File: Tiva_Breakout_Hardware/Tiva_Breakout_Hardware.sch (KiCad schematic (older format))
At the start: 10 parts, among them U1 TM4C129E_Launchpad

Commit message: Removed unnecessary connectors in schematic to reflect other boards
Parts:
- removed ConnA1, ConnA2: Molex_SL_09, MRDT_Connectors:MOLEX_SL_09_Horizontal, symbol MRDT_Connectors:Molex_SL_09
- removed ConnB1, ConnB2, ConnD1, ConnD2: Molex_SL_08, MRDT_Connectors:MOLEX_SL_08_Horizontal, symbol MRDT_Connectors:Molex_SL_08
- removed ConnC2: Molex_SL_10, MRDT_Connectors:MOLEX_SL_10_Horizontal, symbol MRDT_Connectors:Molex_SL_10
- added 12V_B2: Molex_SL_04, MRDT_Connectors:MOLEX_SL_04_Horizontal, symbol Tiva_Breakout_Hardware-rescue:Molex_SL_04-MRDT_Connectors
- added 30V_A1, 30V_B1: Molex_SL_07, MRDT_Connectors:MOLEX_SL_07_Horizontal, symbol Tiva_Breakout_Hardware-rescue:Molex_SL_07-MRDT_Connectors
- ConnC1: symbol MRDT_Connectors:Molex_SL_10 -> Tiva_Breakout_Hardware-rescue:Molex_SL_10-MRDT_Connectors
- ConnIN1: symbol MRDT_Connectors:Molex_SL_04 -> Tiva_Breakout_Hardware-rescue:Molex_SL_04-MRDT_Connectors
- U1: symbol MRDT_Shields:TM4C129E_Launchpad -> Tiva_Breakout_Hardware-rescue:TM4C129E_Launchpad-MRDT_Shields
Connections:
- wire segments 112 -> 50
- no-connect marks 2 -> 44

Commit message: rearranged pcb to account for physical layout
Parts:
- removed 30V_A1, 30V_B1: Molex_SL_07, MRDT_Connectors:MOLEX_SL_07_Horizontal, symbol Tiva_Breakout_Hardware-rescue:Molex_SL_07-MRDT_Connectors
- added Conn30V_L1, Conn30V_R1: Molex_SL_08, MRDT_Connectors:MOLEX_SL_08_Horizontal, symbol MRDT_Connectors:Molex_SL_08
- renumbered ConnC1 to ConnPCH_C2
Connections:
- no-connect marks 44 -> 46
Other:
- moved on the sheet: ConnPCH_C2, U1C
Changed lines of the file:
@@
 	3700 1950 4300 1950
 Wire Wire Line
-	3700 2050 4300 2050
-Wire Wire Line
-	5950 1350 6400 1350
-Wire Wire Line
-	5950 1450 6400 1450
-Wire Wire Line
-	5950 1550 6400 1550
-Wire Wire Line
-	5950 1650 6400 1650
-Wire Wire Line
-	5950 1750 6400 1750
-Wire Wire Line
-	5950 1850 6400 1850
-Wire Wire Line
-	5950 1950 6400 1950
-Wire Wire Line
-	5950 2050 6400 2050
-Wire Wire Line
-	5950 2150 6400 2150
-Wire Wire Line
-	5950 2250 6400 2250
+	6000 3000 6450 3000
+Wire Wire Line
+	6000 3100 6450 3100
+Wire Wire Line
+	6000 3200 6450 3200
+Wire Wire Line
+	6000 3300 6450 3300
+Wire Wire Line
+	6000 3400 6450 3400
+Wire Wire Line
+	6000 3500 6450 3500
+Wire Wire Line
+	6000 3600 6450 3600
+Wire Wire Line
+	6000 3700 6450 3700
+Wire Wire Line
+	6000 3800 6450 3800
+Wire Wire Line
+	6000 3900 6450 3900
 Wire Wire Line
 	4300 3200 3700 3200
@@
 L Tiva_Breakout_Hardware-rescue:TM4C129E_Launchpad-MRDT_Shields U1
 U 3 1 5D8F4A55
-P 6600 2300
-F 0 "U1" H 6650 3450 60  0000 L CNN
-F 1 "TM4C129E_Launchpad" V 6950 2350 60  0000 L CNN
-F 2 "MRDT_Shields:Tiva_Breakout" H 6600 2300 60  0001 C CNN
-F 3 "" H 6600 2300 60  0001 C CNN
-	3    6600 2300
+P 6650 2150
+F 0 "U1" H 6700 3300 60  0000 L CNN
+F 1 "TM4C129E_Launchpad" V 7000 2200 60  0000 L CNN
+F 2 "MRDT_Shields:Tiva_Breakout" H 6650 2150 60  0001 C CNN
+F 3 "" H 6650 2150 60  0001 C CNN
+	3    6650 2150
 	1    0    0    -1
 $EndComp
@@
 $EndComp
 $Comp
-L Tiva_Breakout_Hardware-rescue:Molex_SL_10-MRDT_Connectors ConnC1
+L Tiva_Breakout_Hardware-rescue:Molex_SL_10-MRDT_Connectors ConnPCH_C2
 U 1 1 5D908EEE
-P 5750 2300
-F 0 "ConnC1" H 5692 3497 60  0000 C CNN
-F 1 "Molex_SL_10" H 5692 3391 60  0000 C CNN
-F 2 "MRDT_Connectors:MOLEX_SL_10_Horizontal" H 5750 2800 60  0001 C CNN
-F 3 "" H 5750 2800 60  0001 C CNN
-	1    5750 2300
+P 5800 3950
+F 0 "ConnPCH_C2" H 5742 5147 60  0000 C CNN
+F 1 "Molex_SL_10" H 5742 5041 60  0000 C CNN
+F 2 "MRDT_Connectors:MOLEX_SL_10_Horizontal" H 5800 4450 60  0001 C CNN
+F 3 "" H 5800 4450 60  0001 C CNN
+	1    5800 3950
 	-1   0    0    -1
 $EndComp
@@
 NoConn ~ 8600 2150
 NoConn ~ 8600 2250
-NoConn ~ 6450 3000
-NoConn ~ 6450 3100
-NoConn ~ 6450 3200
-NoConn ~ 6450 3300
-NoConn ~ 6450 3400
-NoConn ~ 6450 3500
-NoConn ~ 6450 3600
-NoConn ~ 6450 3700
-NoConn ~ 6450 3800
-NoConn ~ 6450 3900
 NoConn ~ 8650 3900
 NoConn ~ 8650 3800
@@
 Text Notes 7800 850  0    197  ~ 39
 Unassigned
-$Comp
-L Tiva_Breakout_Hardware-rescue:Molex_SL_07-MRDT_Connectors 30V_A1
-U 1 1 5DBFC3B6
-P 950 2000
-F 0 "30V_A1" H 892 2897 60  0000 C CNN
-F 1 "Molex_SL_07" H 892 2791 60  0000 C CNN
-F 2 "MRDT_Connectors:MOLEX_SL_07_Horizontal" H 950 2200 60  0001 C CNN
-F 3 "" H 950 2200 60  0001 C CNN
-	1    950  2000
-	-1   0    0    -1
-$EndComp
-NoConn ~ 3700 2150
 NoConn ~ 1500 2150
+Wire Wire Line
+	1150 1350 1500 1350
+Wire Wire Line
+	1500 1450 1150 1450
+Wire Wire Line
+	1150 1550 1500 1550
+Wire Wire Line
+	1500 1650 1150 1650
+Wire Wire Line
+	1150 1750 1500 1750
+Wire Wire Line
+	1500 1850 1150 1850
+$Comp
+L MRDT_Connectors:Molex_SL_08 Conn30V_L1
+U 1 1 5DCE1DDF
+P 950 2100
+F 0 "Conn30V_L1" H 892 3097 60  0000 C CNN
+F 1 "Molex_SL_08" H 892 2991 60  0000 C CNN
+F 2 "MRDT_Connectors:MOLEX_SL_08_Horizontal" H 950 2400 60  0001 C CNN
+F 3 "" H 950 2400 60  0001 C CNN
+	1    950  2100
+	-1   0    0    -1
+$EndComp
+$Comp
+L MRDT_Connectors:Molex_SL_08 Conn30V_R1
+U 1 1 5DCE5C02
+P 4500 2200
+F 0 "Conn30V_R1" H 4628 2658 60  0000 L CNN
+F 1 "Molex_SL_08" H 4628 2552 60  0000 L CNN
+F 2 "MRDT_Connectors:MOLEX_SL_08_Horizontal" H 4500 2500 60  0001 C CNN
+F 3 "" H 4500 2500 60  0001 C CNN
+	1    4500 2200
+	1    0    0    -1
+$EndComp
+Wire Wire Line
+	3700 2050 4300 2050
+Wire Wire Line
+	3700 2150 4300 2150
+NoConn ~ 1500 1950
 NoConn ~ 1500 2050
-Wire Wire Line
-	1150 1350 1500 1350
-Wire Wire Line
-	1500 1450 1150 1450
-Wire Wire Line
-	1150 1550 1500 1550
-Wire Wire Line
-	1500 1650 1150 1650
-Wire Wire Line
-	1150 1750 1500 1750
-Wire Wire Line
-	1500 1850 1150 1850
-Wire Wire Line
-	1150 1950 1500 1950
-$Comp
-L Tiva_Breakout_Hardware-rescue:Molex_SL_07-MRDT_Connectors 30V_B1
-U 1 1 5DC09C1D
-P 4500 2100
-F 0 "30V_B1" H 4450 3000 60  0000 L CNN
-F 1 "Molex_SL_07" H 4300 2900 60  0000 L CNN
-F 2 "MRDT_Connectors:MOLEX_SL_07_Horizontal" H 4500 2300 60  0001 C CNN
-F 3 "" H 4500 2300 60  0001 C CNN
-	1    4500 2100
-	1    0    0    -1
-$EndComp
+NoConn ~ 1150 2050
+NoConn ~ 1150 1950
+NoConn ~ 6450 1200
+NoConn ~ 6450 1300
+NoConn ~ 6450 1400
+NoConn ~ 6450 1500
+NoConn ~ 6450 1600
+NoConn ~ 6450 1700
+NoConn ~ 6450 1800
+NoConn ~ 6450 1900
+NoConn ~ 6450 2000
+NoConn ~ 6450 2100
 $EndSCHEMATC

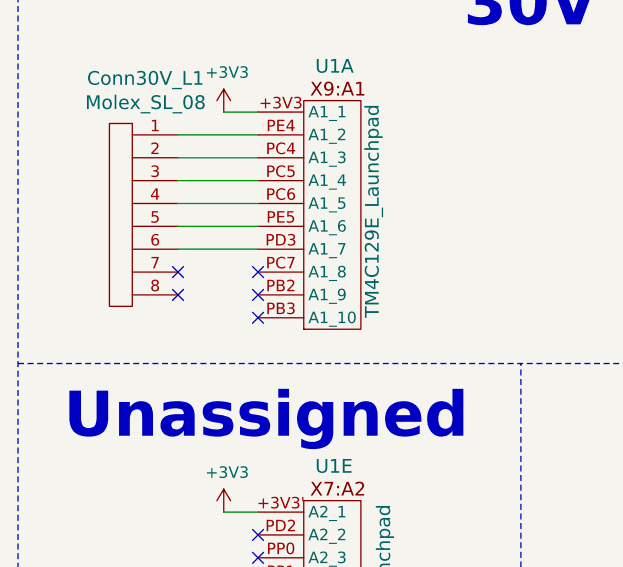
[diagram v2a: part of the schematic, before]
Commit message: In process of changing layout for smaller board
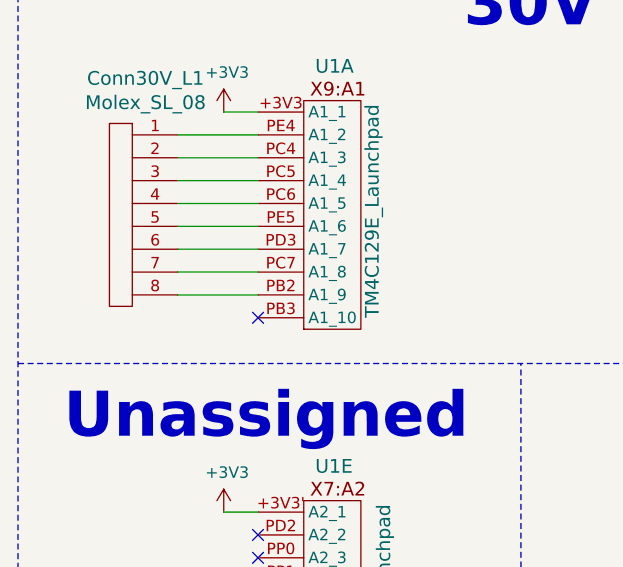
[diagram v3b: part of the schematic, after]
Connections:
- net at U1.PB2 (A1_9): now also Conn30V_L1.8
- net at U1.PC7 (A1_8): now also Conn30V_L1.7
- no-connect marks 46 -> 42
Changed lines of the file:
@@
 	1    0    0    -1
 $EndComp
-Wire Wire Line
-	3700 2050 4300 2050
-Wire Wire Line
-	3700 2150 4300 2150
-NoConn ~ 1500 1950
-NoConn ~ 1500 2050
-NoConn ~ 1150 2050
-NoConn ~ 1150 1950
 NoConn ~ 6450 1200
 NoConn ~ 6450 1300
@@
 NoConn ~ 6450 2000
 NoConn ~ 6450 2100
+Wire Wire Line
+	3700 2050 4300 2050
+Wire Wire Line
+	3700 2150 4300 2150
+Wire Wire Line
+	1150 1950 1500 1950
+Wire Wire Line
+	1150 2050 1500 2050
 $EndSCHEMATC

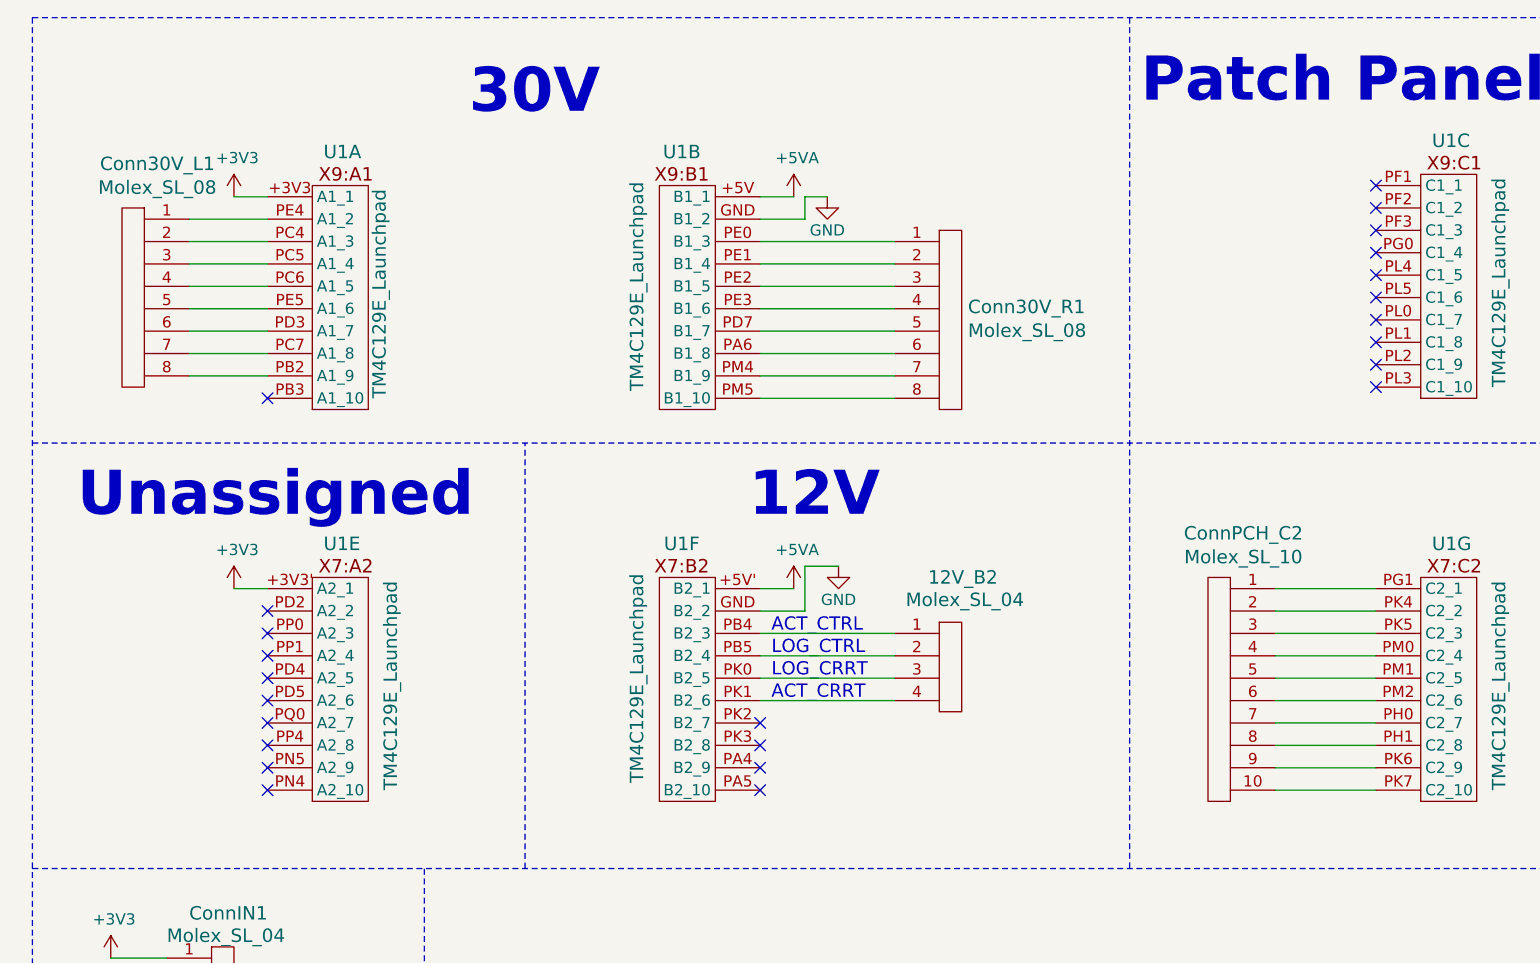
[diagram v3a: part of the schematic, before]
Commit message: New layout, as board is on left of others now. Changed pin assignments.
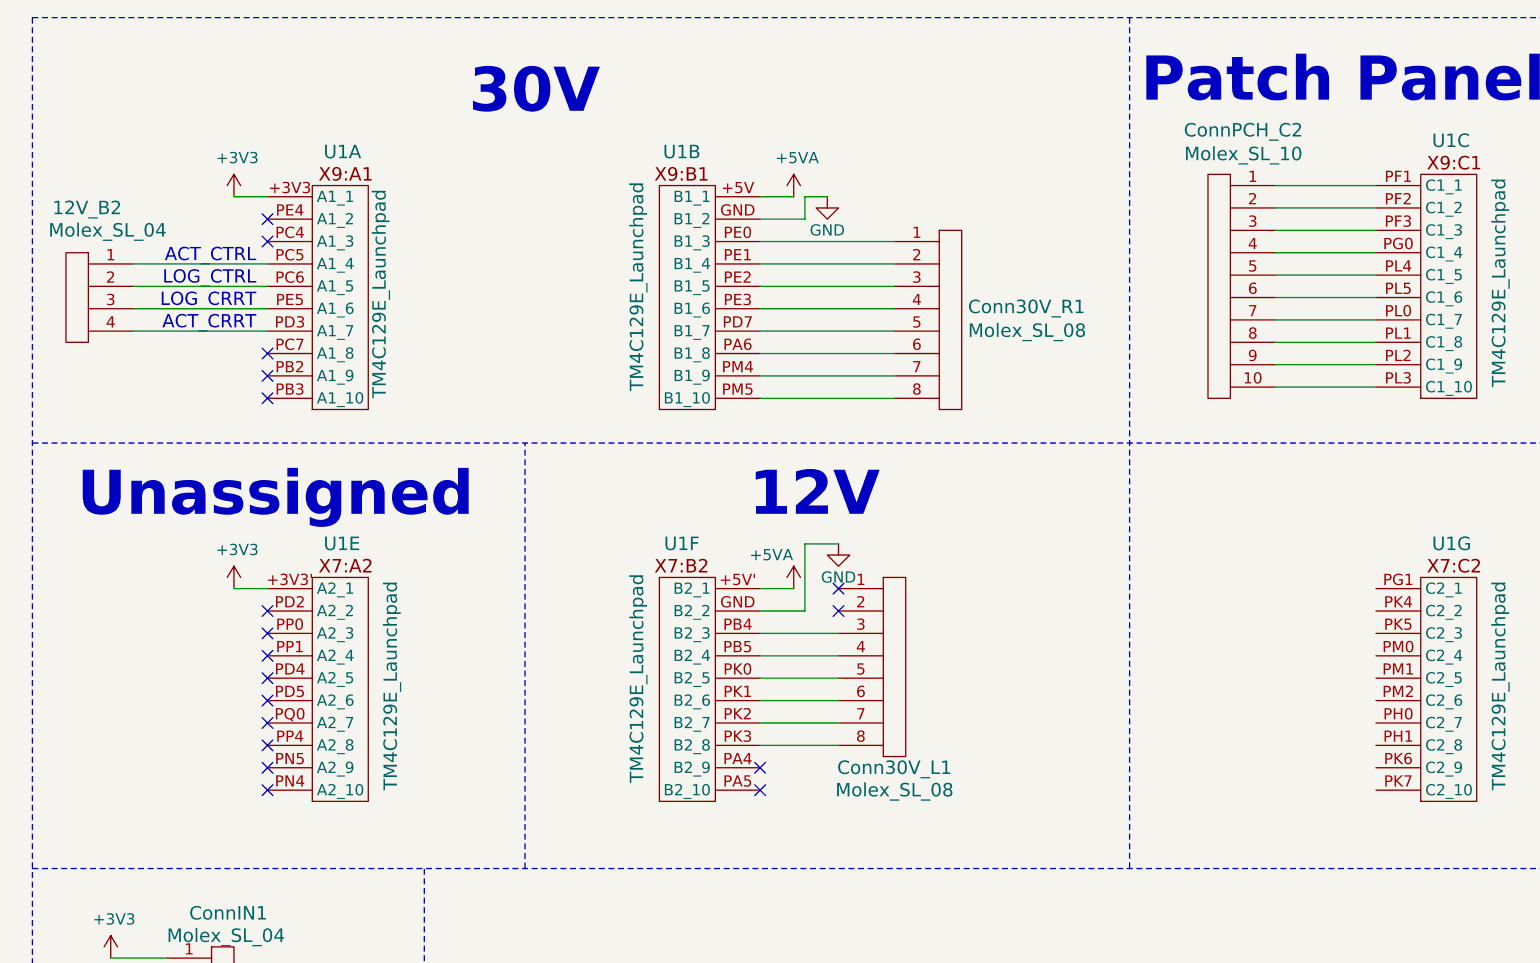
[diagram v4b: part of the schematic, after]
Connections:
- net at U1.PB2 (A1_9): no longer Conn30V_L1.8
- net at U1.PC4 (A1_3): no longer Conn30V_L1.2
- net at U1.PC5 (A1_4): now also 12V_B2.1; no longer Conn30V_L1.3
- net at U1.PC6 (A1_5): now also 12V_B2.2; no longer Conn30V_L1.4
- net at U1.PC7 (A1_8): no longer Conn30V_L1.7
- net at U1.PD3 (A1_7): now also 12V_B2.4; no longer Conn30V_L1.6
- net at U1.PE4 (A1_2): no longer Conn30V_L1.1
- net at U1.PE5 (A1_6): now also 12V_B2.3; no longer Conn30V_L1.5
- net at U1.PF1 (C1_1): now also ConnPCH_C2.1
- net at U1.PF2 (C1_2): now also ConnPCH_C2.2
- net at U1.PF3 (C1_3): now also ConnPCH_C2.3
- net at U1.PG0 (C1_4): now also ConnPCH_C2.4
- net at U1.PL0 (C1_7): now also ConnPCH_C2.7
- net at U1.PL1 (C1_8): now also ConnPCH_C2.8
- net at U1.PL2 (C1_9): now also ConnPCH_C2.9
- net at U1.PL3 (C1_10): now also ConnPCH_C2.10
- net at U1.PL4 (C1_5): now also ConnPCH_C2.5
- net at U1.PL5 (C1_6): now also ConnPCH_C2.6
- net at U1.PB4 (B2_3): now also Conn30V_L1.3; no longer 12V_B2.1
- net at U1.PB5 (B2_4): now also Conn30V_L1.4; no longer 12V_B2.2
- net at U1.PK0 (B2_5): now also Conn30V_L1.5; no longer 12V_B2.3
- net at U1.PK1 (B2_6): now also Conn30V_L1.6; no longer 12V_B2.4
- net at U1.PK2 (B2_7): now also Conn30V_L1.7
- net at U1.PK3 (B2_8): now also Conn30V_L1.8
- net at U1.PG1 (C2_1): no longer ConnPCH_C2.1
- net at U1.PH0 (C2_7): no longer ConnPCH_C2.7
- net at U1.PH1 (C2_8): no longer ConnPCH_C2.8
- net at U1.PK4 (C2_2): no longer ConnPCH_C2.2
- net at U1.PK5 (C2_3): no longer ConnPCH_C2.3
- net at U1.PK6 (C2_9): no longer ConnPCH_C2.9
- net at U1.PK7 (C2_10): no longer ConnPCH_C2.10
- net at U1.PM0 (C2_4): no longer ConnPCH_C2.4
- net at U1.PM1 (C2_5): no longer ConnPCH_C2.5
- net at U1.PM2 (C2_6): no longer ConnPCH_C2.6
- no-connect marks 42 -> 36
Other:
- moved on the sheet: 12V_B2, Conn30V_L1, ConnPCH_C2
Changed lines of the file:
@@
 Text Notes 800  5750 0    118  ~ 24
 Power Input
-NoConn ~ 8600 1750
 NoConn ~ 8650 3400
 $Comp
@@
 P 3850 3000
 F 0 "#PWR0104" H 3850 2850 50  0001 C CNN
-F 1 "+5VA" H 3865 3173 50  0000 C CNN
+F 1 "+5VA" H 3750 3150 50  0000 C CNN
 F 2 "" H 3850 3000 50  0001 C CNN
 F 3 "" H 3850 3000 50  0001 C CNN
@@
 L power:GND #PWR0110
 U 1 1 5D93847D
-P 4050 2900
-F 0 "#PWR0110" H 4050 2650 50  0001 C CNN
-F 1 "GND" H 4050 2750 50  0000 C CNN
-F 2 "" H 4050 2900 50  0001 C CNN
-F 3 "" H 4050 2900 50  0001 C CNN
-	1    4050 2900
+P 4050 2800
+F 0 "#PWR0110" H 4050 2550 50  0001 C CNN
+F 1 "GND" H 4050 2650 50  0000 C CNN
+F 2 "" H 4050 2800 50  0001 C CNN
+F 3 "" H 4050 2800 50  0001 C CNN
+	1    4050 2800
 	1    0    0    -1
 $EndComp
@@
 	3700 1950 4300 1950
 Wire Wire Line
-	6000 3000 6450 3000
-Wire Wire Line
-	6000 3100 6450 3100
-Wire Wire Line
-	6000 3200 6450 3200
-Wire Wire Line
-	6000 3300 6450 3300
-Wire Wire Line
-	6000 3400 6450 3400
-Wire Wire Line
-	6000 3500 6450 3500
-Wire Wire Line
-	6000 3600 6450 3600
-Wire Wire Line
-	6000 3700 6450 3700
-Wire Wire Line
-	6000 3800 6450 3800
-Wire Wire Line
-	6000 3900 6450 3900
-Wire Wire Line
-	4300 3200 3700 3200
-Wire Wire Line
-	3700 3300 4300 3300
-Wire Wire Line
-	3700 3400 4300 3400
-Wire Wire Line
-	3700 3500 4300 3500
+	6000 1200 6450 1200
+Wire Wire Line
+	6000 1300 6450 1300
+Wire Wire Line
+	6000 1400 6450 1400
+Wire Wire Line
+	6000 1500 6450 1500
+Wire Wire Line
+	6000 1600 6450 1600
+Wire Wire Line
+	6000 1700 6450 1700
+Wire Wire Line
+	6000 1800 6450 1800
+Wire Wire Line
+	6000 1900 6450 1900
+Wire Wire Line
+	6000 2000 6450 2000
+Wire Wire Line
+	6000 2100 6450 2100
 $Comp
 L Tiva_Breakout_Hardware-rescue:TM4C129E_Launchpad-MRDT_Shields U1
@@
 	3    6650 2150
 	1    0    0    -1
-$EndComp
-$Comp
-L Tiva_Breakout_Hardware-rescue:TM4C129E_Launchpad-MRDT_Shields U1
-U 4 1 5D8F6A14
-P 8400 2300
-F 0 "U1" H 8550 3450 60  0000 C CNN
-F 1 "TM4C129E_Launchpad" V 8750 2850 60  0000 C CNN
-F 2 "MRDT_Shields:Tiva_Breakout" H 8400 2300 60  0001 C CNN
-F 3 "" H 8400 2300 60  0001 C CNN
-	4    8400 2300
-	-1   0    0    -1
 $EndComp
 $Comp
@@
 L Tiva_Breakout_Hardware-rescue:Molex_SL_10-MRDT_Connectors ConnPCH_C2
 U 1 1 5D908EEE
-P 5800 3950
-F 0 "ConnPCH_C2" H 5742 5147 60  0000 C CNN
-F 1 "Molex_SL_10" H 5742 5041 60  0000 C CNN
-F 2 "MRDT_Connectors:MOLEX_SL_10_Horizontal" H 5800 4450 60  0001 C CNN
-F 3 "" H 5800 4450 60  0001 C CNN
-	1    5800 3950
+P 5800 2150
+F 0 "ConnPCH_C2" H 5742 3347 60  0000 C CNN
+F 1 "Molex_SL_10" H 5742 3241 60  0000 C CNN
+F 2 "MRDT_Connectors:MOLEX_SL_10_Horizontal" H 5800 2650 60  0001 C CNN
+F 3 "" H 5800 2650 60  0001 C CNN
+	1    5800 2150
 	-1   0    0    -1
 $EndComp
@@
 12V
 Wire Wire Line
-	3900 2900 4050 2900
-Wire Wire Line
-	3900 2900 3900 3100
-Text Notes 3750 3200 0    59   ~ 0
-ACT_CTRL
-Text Notes 3750 3300 0    59   ~ 0
-LOG_CTRL
-Text Notes 3750 3400 0    59   ~ 0
-LOG_CRRT
-Text Notes 3750 3500 0    59   ~ 0
-ACT_CRRT
+	3900 2800 4050 2800
 Text Notes 5400 850  0    197  ~ 39
 Patch Panel
@@
 Wire Notes Line
 	450  450  10250 450
-$Comp
-L Tiva_Breakout_Hardware-rescue:Molex_SL_04-MRDT_Connectors 12V_B2
-U 1 1 5DC19990
-P 4500 3550
-F 0 "12V_B2" H 4450 4150 60  0000 L CNN
-F 1 "Molex_SL_04" H 4350 4050 60  0000 L CNN
-F 2 "MRDT_Connectors:MOLEX_SL_04_Horizontal" H 4500 3550 60  0001 C CNN
-F 3 "" H 4500 3550 60  0001 C CNN
-	1    4500 3550
-	1    0    0    -1
-$EndComp
-NoConn ~ 3700 3600
-NoConn ~ 3700 3700
 NoConn ~ 3700 3800
 NoConn ~ 3700 3900
@@
 NoConn ~ 1500 3800
 NoConn ~ 1500 3900
-NoConn ~ 8600 1450
-NoConn ~ 8600 1550
-NoConn ~ 8600 1650
-NoConn ~ 8600 1850
-NoConn ~ 8600 1950
-NoConn ~ 8600 2050
-NoConn ~ 8600 2150
-NoConn ~ 8600 2250
 NoConn ~ 8650 3900
 NoConn ~ 8650 3800
@@
 NoConn ~ 1500 2150
 Wire Wire Line
-	1150 1350 1500 1350
-Wire Wire Line
-	1500 1450 1150 1450
-Wire Wire Line
-	1150 1550 1500 1550
-Wire Wire Line
-	1500 1650 1150 1650
-Wire Wire Line
-	1150 1750 1500 1750
-Wire Wire Line
-	1500 1850 1150 1850
+	4050 3200 3700 3200
+Wire Wire Line
+	3700 3300 4050 3300
+Wire Wire Line
+	4050 3400 3700 3400
+Wire Wire Line
+	3700 3500 4050 3500
+Wire Wire Line
+	4050 3600 3700 3600
+Wire Wire Line
+	3700 3700 4050 3700
 $Comp
 L MRDT_Connectors:Molex_SL_08 Conn30V_L1
 U 1 1 5DCE1DDF
-P 950 2100
-F 0 "Conn30V_L1" H 892 3097 60  0000 C CNN
-F 1 "Molex_SL_08" H 892 2991 60  0000 C CNN
-F 2 "MRDT_Connectors:MOLEX_SL_08_Horizontal" H 950 2400 60  0001 C CNN
-F 3 "" H 950 2400 60  0001 C CNN
-	1    950  2100
-	-1   0    0    -1
+P 4250 3750
+F 0 "Conn30V_L1" H 4300 3700 60  0000 C CNN
+F 1 "Molex_SL_08" H 4300 3600 60  0000 C CNN
+F 2 "MRDT_Connectors:MOLEX_SL_08_Horizontal" H 4250 4050 60  0001 C CNN
+F 3 "" H 4250 4050 60  0001 C CNN
+	1    4250 3750
+	1    0    0    -1
 $EndComp
 $Comp
@@
 	1    0    0    -1
 $EndComp
-NoConn ~ 6450 1200
-NoConn ~ 6450 1300
-NoConn ~ 6450 1400
-NoConn ~ 6450 1500
-NoConn ~ 6450 1600
-NoConn ~ 6450 1700
-NoConn ~ 6450 1800
-NoConn ~ 6450 1900
-NoConn ~ 6450 2000
-NoConn ~ 6450 2100
 Wire Wire Line
 	3700 2050 4300 2050
 Wire Wire Line
 	3700 2150 4300 2150
-Wire Wire Line
-	1150 1950 1500 1950
-Wire Wire Line
-	1150 2050 1500 2050
+NoConn ~ 4050 3000
+NoConn ~ 4050 3100
+Wire Wire Line
+	3900 2800 3900 3100
+NoConn ~ 1500 1950
+NoConn ~ 1500 2050
+NoConn ~ 1500 1450
+NoConn ~ 1500 1350
+NoConn ~ 8600 2250
+NoConn ~ 8600 2150
+NoConn ~ 8600 2050
+NoConn ~ 8600 1950
+NoConn ~ 8600 1850
+NoConn ~ 8600 1650
+NoConn ~ 8600 1550
+NoConn ~ 8600 1450
+NoConn ~ 8600 1750
+$Comp
+L Tiva_Breakout_Hardware-rescue:TM4C129E_Launchpad-MRDT_Shields U1
+U 4 1 5D8F6A14
+P 8400 2300
+F 0 "U1" H 8550 3450 60  0000 C CNN
+F 1 "TM4C129E_Launchpad" V 8750 2850 60  0000 C CNN
+F 2 "MRDT_Shields:Tiva_Breakout" H 8400 2300 60  0001 C CNN
+F 3 "" H 8400 2300 60  0001 C CNN
+	4    8400 2300
+	-1   0    0    -1
+$EndComp
+$Comp
+L Tiva_Breakout_Hardware-rescue:Molex_SL_04-MRDT_Connectors 12V_B2
+U 1 1 5DC19990
+P 700 1900
+F 0 "12V_B2" H 550 2500 60  0000 L CNN
+F 1 "Molex_SL_04" H 350 2400 60  0000 L CNN
+F 2 "MRDT_Connectors:MOLEX_SL_04_Horizontal" H 700 1900 60  0001 C CNN
+F 3 "" H 700 1900 60  0001 C CNN
+	1    700  1900
+	-1   0    0    -1
+$EndComp
+Text Notes 1450 1850 2    59   ~ 0
+ACT_CRRT
+Text Notes 1450 1750 2    59   ~ 0
+LOG_CRRT
+Text Notes 1450 1650 2    59   ~ 0
+LOG_CTRL
+Text Notes 1450 1550 2    59   ~ 0
+ACT_CTRL
+Wire Wire Line
+	1500 1850 900  1850
+Wire Wire Line
+	1500 1750 900  1750
+Wire Wire Line
+	1500 1650 900  1650
+Wire Wire Line
+	900  1550 1500 1550
 $EndSCHEMATC
